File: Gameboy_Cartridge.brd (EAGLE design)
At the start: 49.3 x 48 mm, 10 parts, among them IC1 AT49F040J

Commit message: Fixed most of the issues and routed most of it
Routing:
- net B: track 7.75 -> 54.3 mm
- net 19: track 43.3 -> 84.6 mm, vias 2 -> 4
- net 6: track 7.15 -> 43.5 mm, vias 0 -> 2

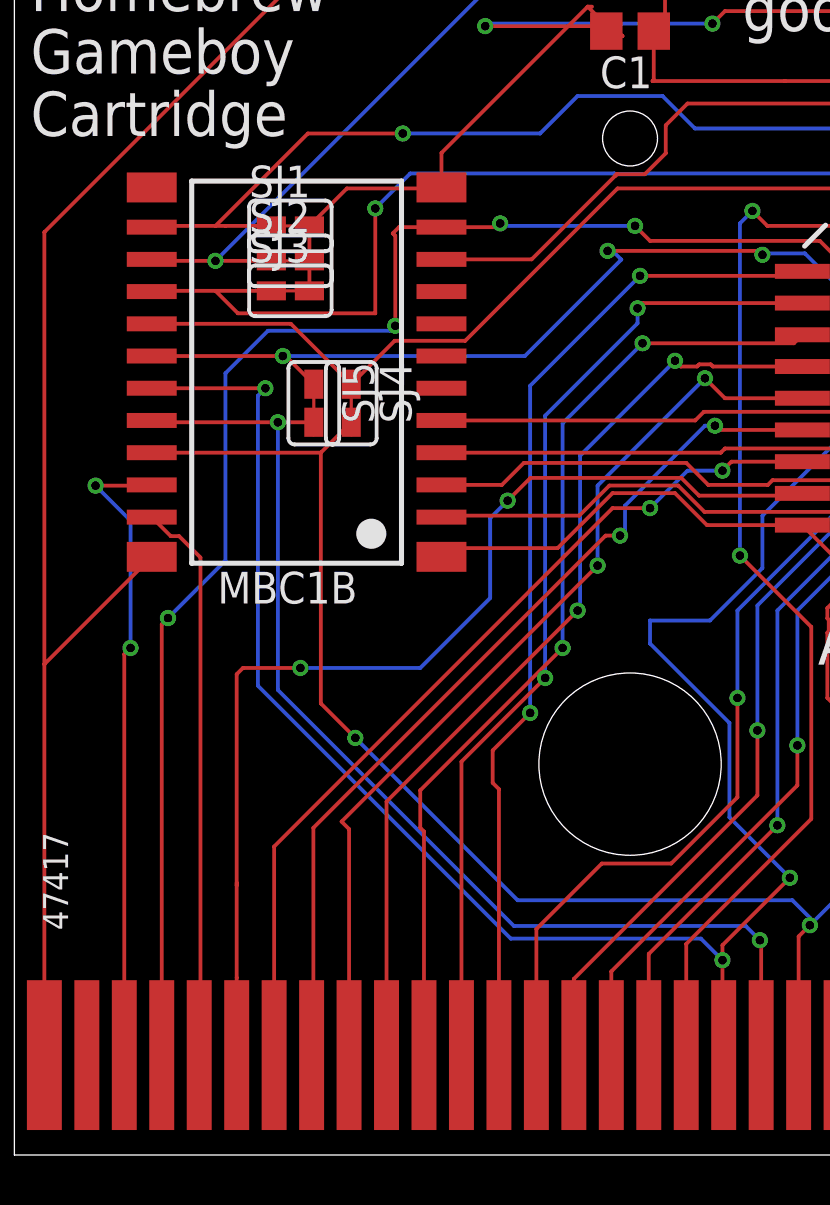
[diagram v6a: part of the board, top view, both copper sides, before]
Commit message: Improve the solder jumper footprint
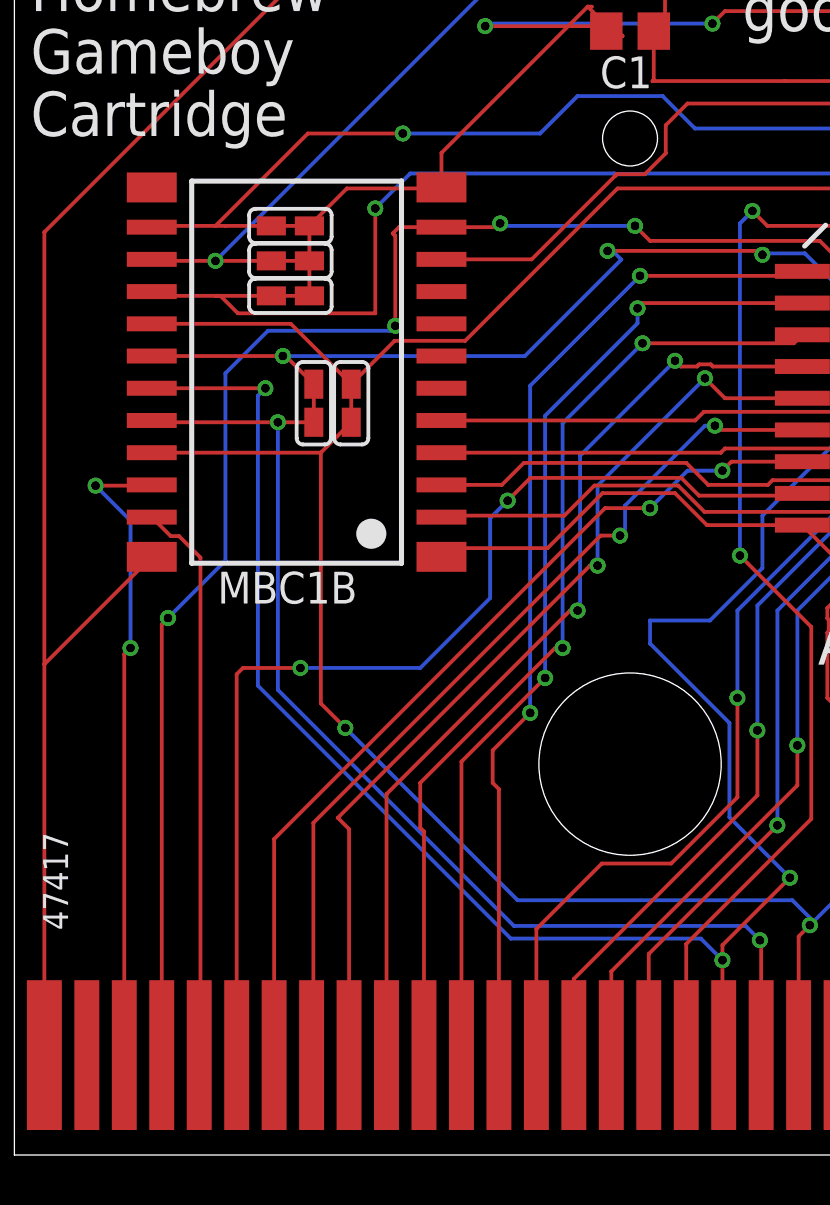
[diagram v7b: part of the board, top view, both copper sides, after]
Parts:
- moved SJ3 0.20 mm to (11.9, 34.4)

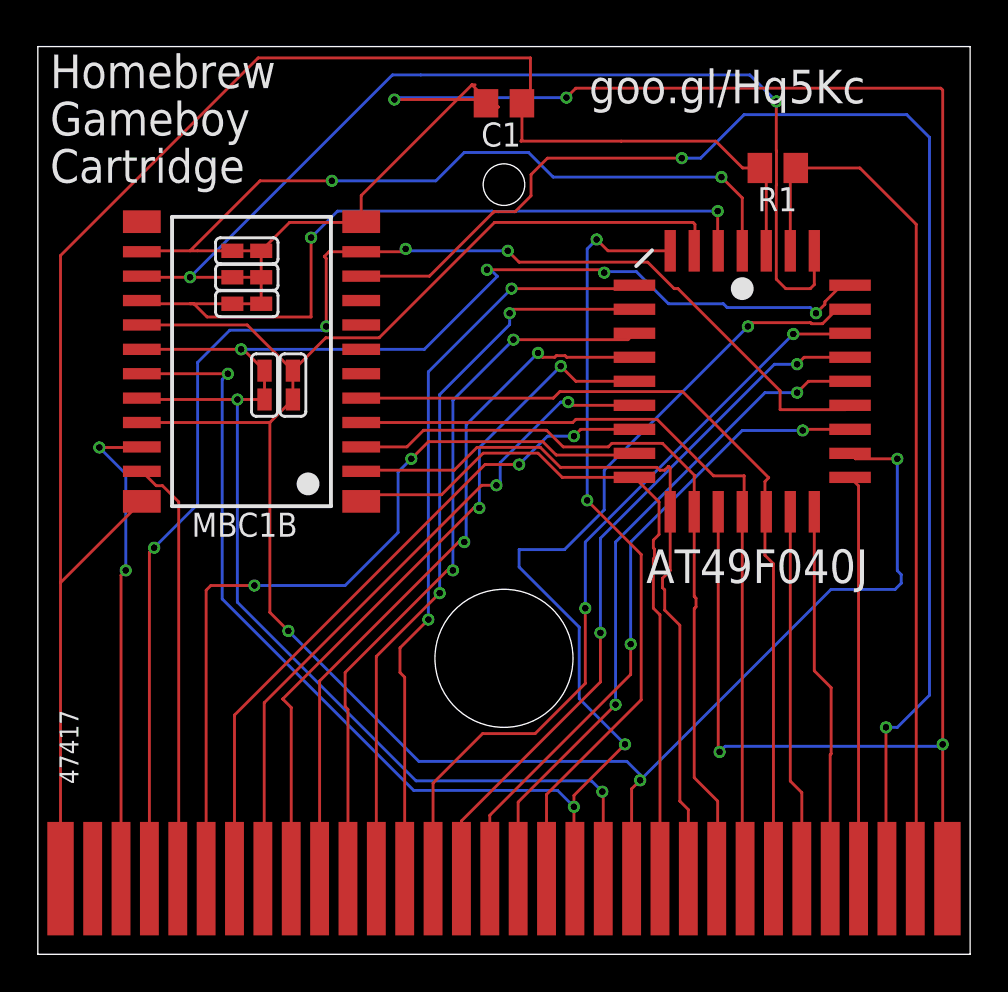
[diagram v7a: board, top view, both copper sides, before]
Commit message: clean up a ton of traces
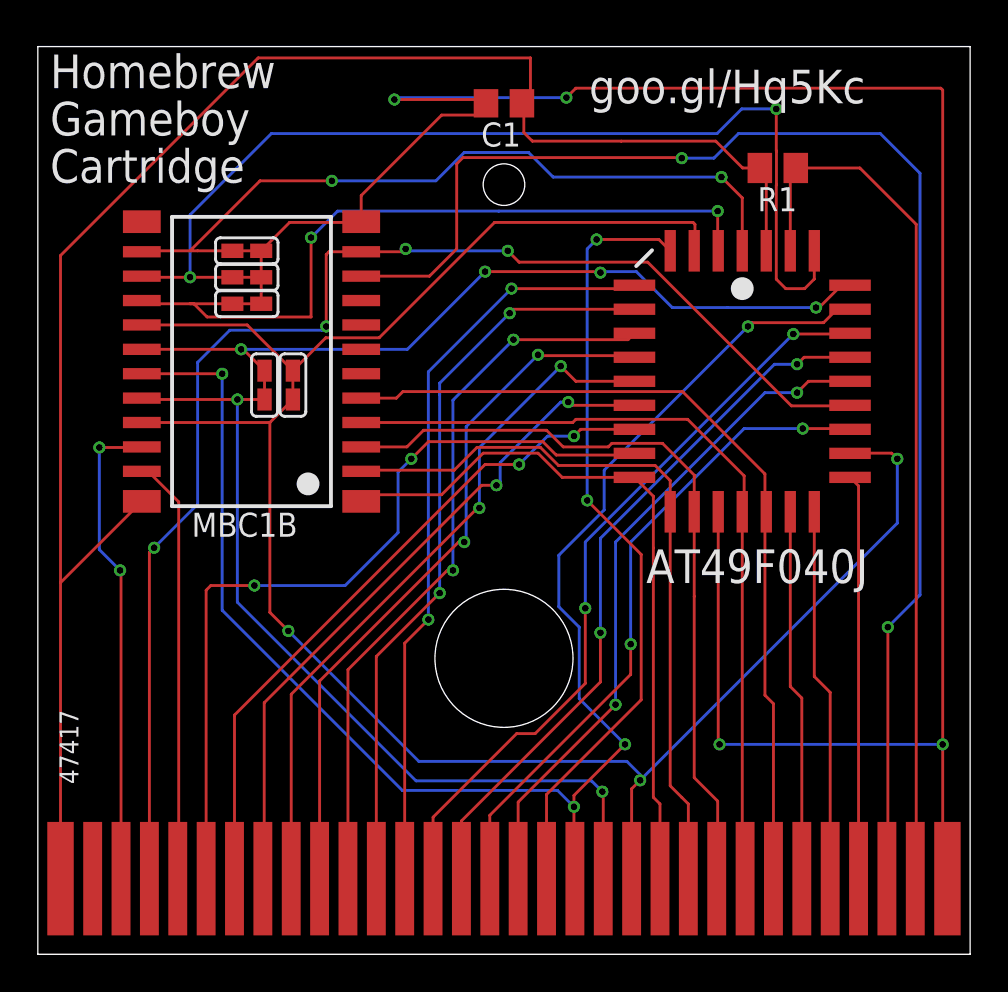
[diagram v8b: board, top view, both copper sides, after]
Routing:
- net 19: track 84.6 -> 81.4 mm
- net GND: track 122.1 -> 119.1 mm
- net 21: track 74.8 -> 72.6 mm
- net E: track 43.7 -> 42.2 mm
- net 30: track 76.5 -> 75.3 mm
- net 14: track 41.3 -> 40.3 mm
- net 23: track 40.3 -> 39.4 mm
- net 4: track 72.2 -> 71.4 mm
